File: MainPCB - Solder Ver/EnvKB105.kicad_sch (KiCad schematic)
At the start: 270 parts, among them J1 Conn_01x05, J5 Conn_01x03_Male, SW1 SW_Push, SW2 SW_Push, U1 STM32F401RCTx, U2 SPX3819M5-L-3-3, Y1 8Mhz 3224 4P

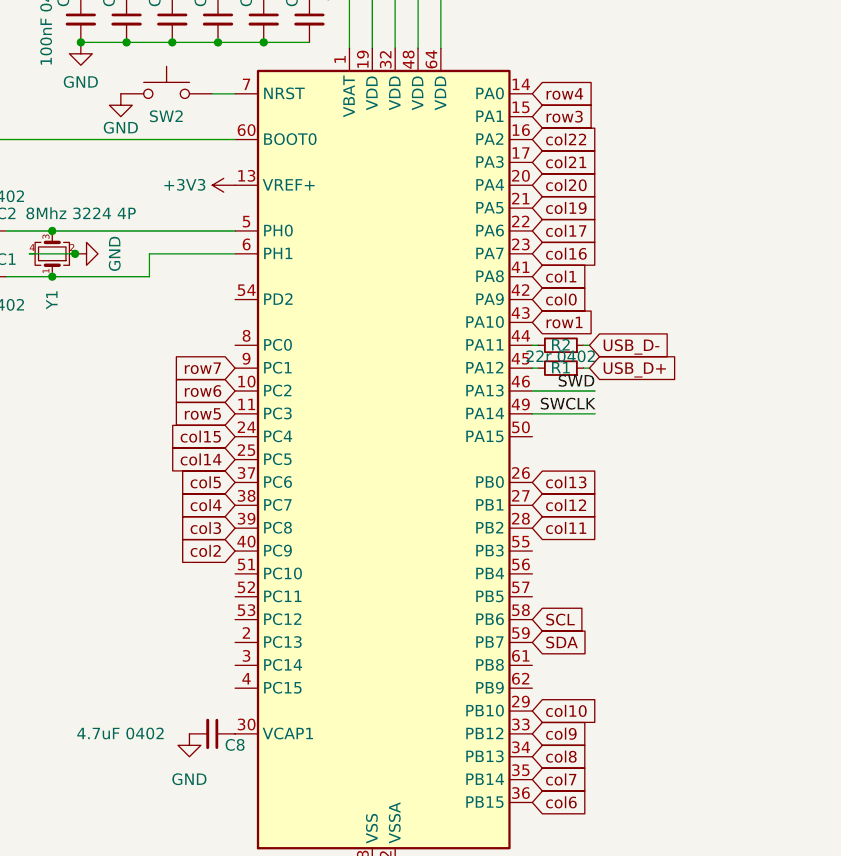
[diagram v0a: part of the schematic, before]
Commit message: tweaked a couple connections to avoid problems
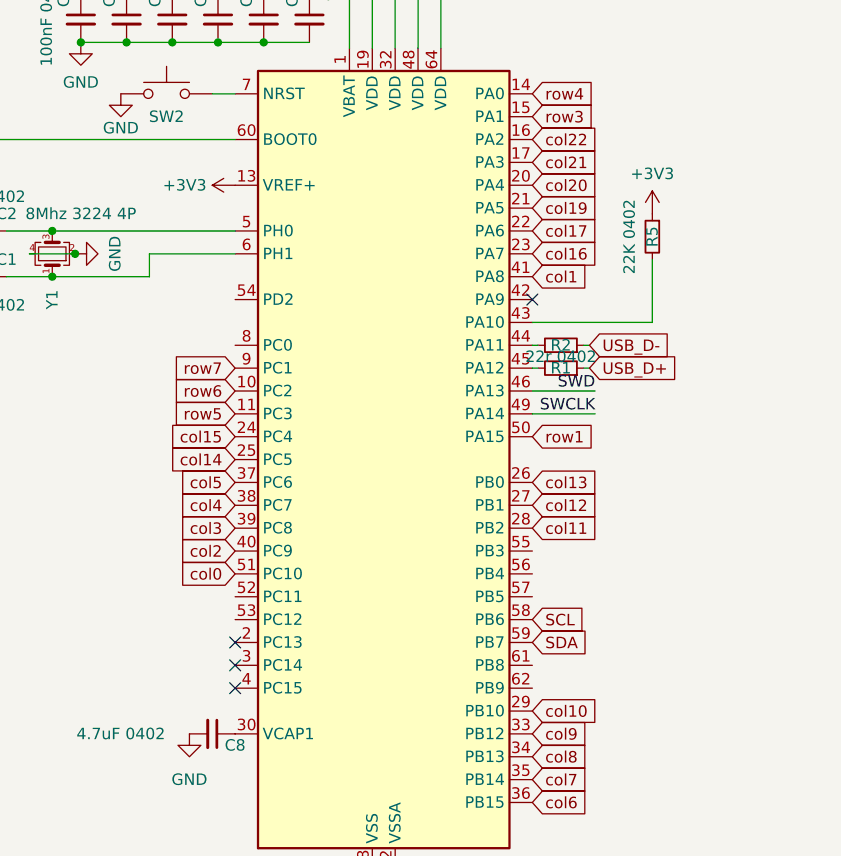
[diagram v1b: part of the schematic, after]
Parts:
- added R5: 22K 0402, Resistor_SMD:R_0402_1005Metric, symbol Device:R_Small
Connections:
- net +3V3: now also R5.1
- net col0: now also U1.51 (PC10); no longer U1.42 (PA9)
- net row1: now also U1.50 (PA15); no longer U1.43 (PA10)
- new net: R5.2, U1.43 (PA10)
- no-connect marks 3 -> 7
